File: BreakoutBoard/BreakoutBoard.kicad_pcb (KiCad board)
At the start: 2 copper layers, 49.5 x 53.3 mm, 32 parts, among them J1 addon_conn, J2 Power_top, J3 Power_bottom, J4 Conn_01x09, J5 Conn_01x10

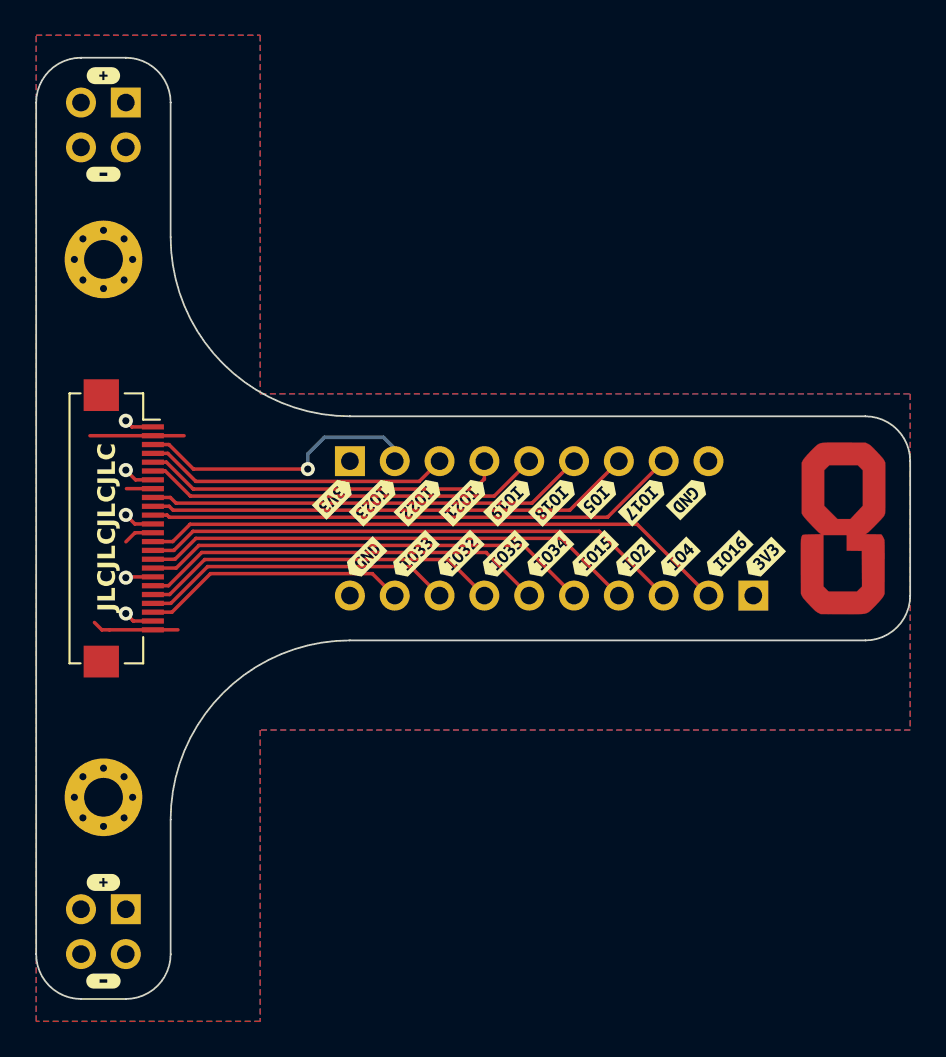
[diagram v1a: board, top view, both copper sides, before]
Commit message: Adapts breakout board to changes in the addon connector
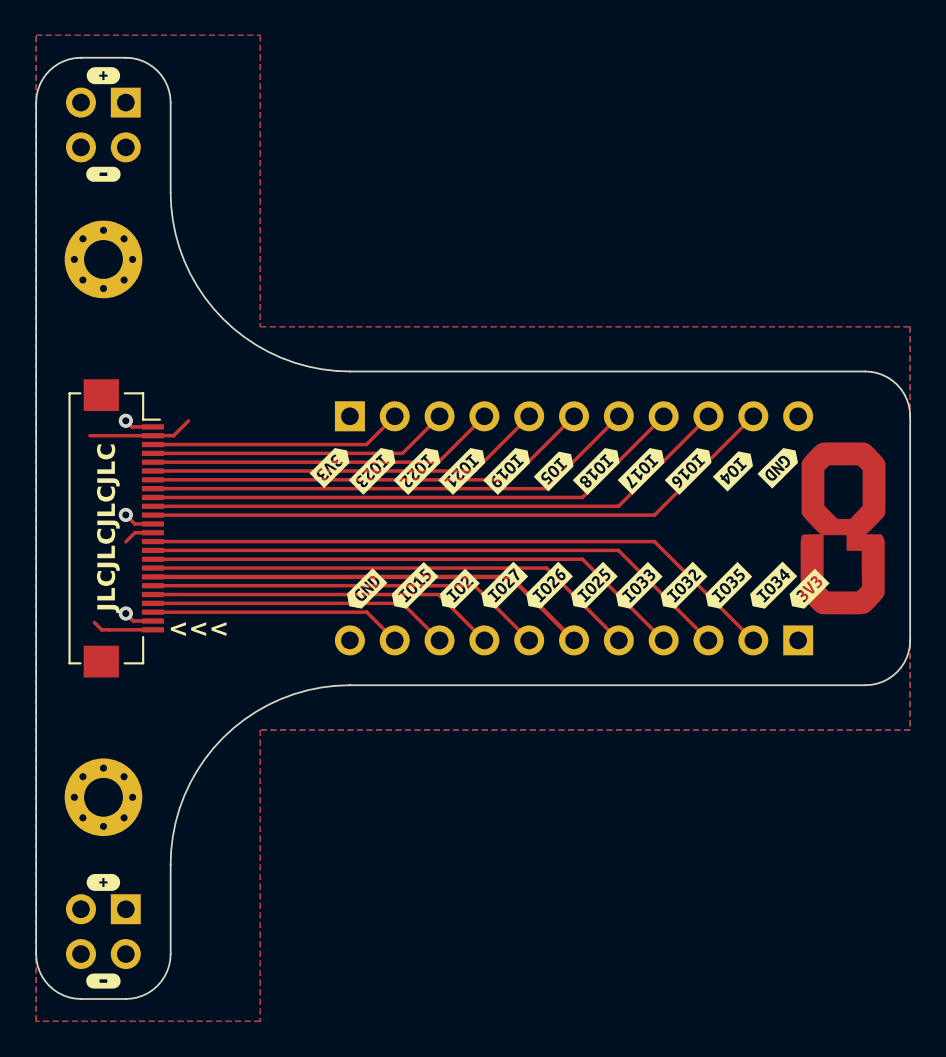
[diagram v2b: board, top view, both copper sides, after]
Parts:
- removed kibuzzard-6259454A: G***, kibuzzard-6259454A
- removed kibuzzard-6259454F: G***, kibuzzard-6259454F
- removed kibuzzard-62594553: G***, kibuzzard-62594553
- removed kibuzzard-62599743: G***, kibuzzard-62599743
- added kibuzzard-62829C43: G***, kibuzzard-62829C43, F.Cu at (164.1, 95.7)
- added kibuzzard-62829C54: G***, kibuzzard-62829C54, F.Cu at (166.6, 95.7)
- added kibuzzard-62829CE0: G***, kibuzzard-62829CE0, F.Cu at (158.5, 102.4)
- added kibuzzard-62829D15: G***, kibuzzard-62829D15, F.Cu at (150.9, 102.6)
- added kibuzzard-62829D2F: G***, kibuzzard-62829D2F, F.Cu at (153.4, 102.4)
- added kibuzzard-62829D34: G***, kibuzzard-62829D34, F.Cu at (156.0, 102.4)
- added kibuzzard-62829E35: G***, kibuzzard-62829E35, B.Cu at (156.2, 99.1)
- J1: footprint GameOver:TXGA_FFC05036-24SBD113W5M_1x24_P0.50mm_Horizontal -> GameOver:Addon_conn_TXGA_FFC05036-24SBD113W5M_1x24_P0.50mm_Horizontal
- J4: value Conn_01x09 -> Conn_01x11; footprint Connector_PinHeader_2.54mm:PinHeader_1x09_P2.54mm_Vertical -> Connector_PinHeader_2.54mm:PinHeader_1x11_P2.54mm_Vertical
- J5: value Conn_01x10 -> Conn_01x11; footprint Connector_PinHeader_2.54mm:PinHeader_1x10_P2.54mm_Vertical -> Connector_PinHeader_2.54mm:PinHeader_1x11_P2.54mm_Vertical
- moved kibuzzard-6259453E 12.8 mm to (166.1, 102.4)
- moved kibuzzard-62594542 12.8 mm to (168.7, 102.4)
- moved kibuzzard-62594532 12.8 mm to (161.0, 102.4)
- moved kibuzzard-6259453A 12.8 mm to (163.6, 102.4)
- moved kibuzzard-62594546 10.4 mm to (148.3, 102.4)
- moved kibuzzard-62594508 5.51 mm to (169.2, 95.5)
- moved J5 3.59 mm to (170.2, 105.4)
- moved kibuzzard-625944FA 3.12 mm to (158.9, 95.7)
- moved kibuzzard-62594559 3.06 mm to (170.7, 102.6)
- moved kibuzzard-625944FF 2.90 mm to (156.5, 95.7)
- moved J4 2.54 mm to (144.8, 92.7)
- moved kibuzzard-6259452C 1.82 mm to (145.6, 102.6)
- moved kibuzzard-625944F4 1.81 mm to (143.8, 95.5)
- moved kibuzzard-625944D4 1.80 mm to (153.8, 95.7)
- moved kibuzzard-625944DF 1.80 mm to (151.3, 95.7)
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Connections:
- J1 pad 10: Net-(J1-IO5) -> Net-(J1-IO16)
- J1 pad 11: Net-(J1-IO17) -> Net-(J1-IO4)
- J1 pad 18: GND -> Net-(J1-IO25)
- J1 pad 19: Net-(J1-IO34) (its old number) -> Net-(J1-IO26)
- J1 pad 20: Net-(J1-IO35) (its old number) -> Net-(J1-IO27)
- J1 pad 21: Net-(J1-IO32) (its old number) -> Net-(J1-IO2)
- J1 pad 22: Net-(J1-IO33) (its old number) -> Net-(J1-IO15)
- J1 pad 7: GND -> Net-(J1-IO5)
- J1 pad 8: +3V3 -> Net-(J1-IO18)
- J1 pad 9: Net-(J1-IO18) -> Net-(J1-IO17)
- J4 pad 6: Net-(J1-IO18) -> Net-(J1-IO5)
- J4 pad 7: Net-(J1-IO5) -> Net-(J1-IO18)
- J4 pad 9: GND -> Net-(J1-IO16)
- J5 pad 10: GND -> Net-(J1-IO15)
- J5 pad 6: Net-(J1-IO34) (its old number) -> Net-(J1-IO25)
- J5 pad 7: Net-(J1-IO35) (its old number) -> Net-(J1-IO26)
- J5 pad 8: Net-(J1-IO32) (its old number) -> Net-(J1-IO27)
- J5 pad 9: Net-(J1-IO33) (its old number) -> Net-(J1-IO2)
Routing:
- net Net-(J1-IO4): track 0.00 -> 36.3 mm
- net Net-(J1-IO16): track 0.00 -> 33.6 mm
- net Net-(J1-IO25): track 0.00 -> 25.4 mm
- net Net-(J1-IO34) (its old number): track 23.1 -> 0.00 mm
- net Net-(J1-IO26): track 0.00 -> 22.6 mm
- net Net-(J1-IO35) (its old number): track 20.5 -> 0.00 mm
- net Net-(J1-IO27): track 0.00 -> 19.9 mm
- net Net-(J1-IO32) (its old number): track 17.8 -> 0.00 mm
- net Net-(J1-IO2): track 0.00 -> 17.1 mm
- net Net-(J1-IO33) (its old number): track 15.1 -> 0.00 mm
- net Net-(J1-IO15): track 0.00 -> 14.4 mm
- net GND: track 8.45 -> 5.14 mm, vias 5 -> 3
- net Net-(J1-IO18): track 25.0 -> 28.1 mm
- net Net-(J1-IO34): track 33.6 -> 36.3 mm
- net Net-(J1-IO35): track 30.9 -> 33.6 mm
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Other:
- outline, holes or cut-outs redrawn

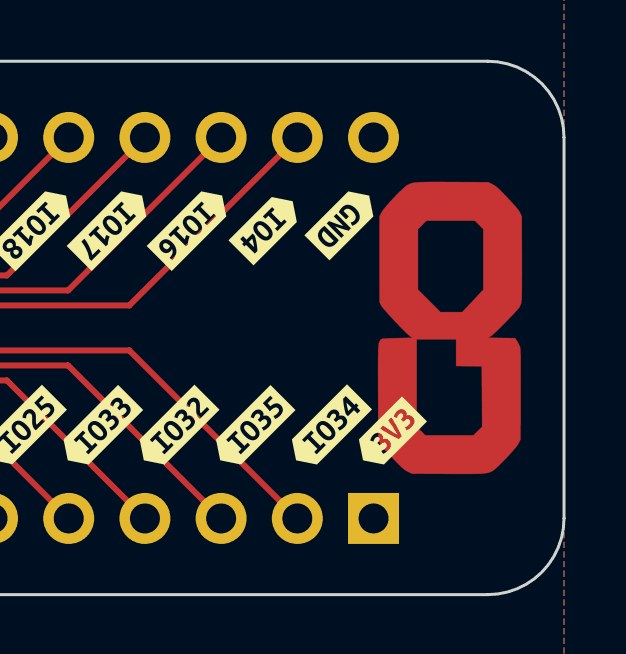
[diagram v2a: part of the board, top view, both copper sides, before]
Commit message: Adds logo to breakout board schematics
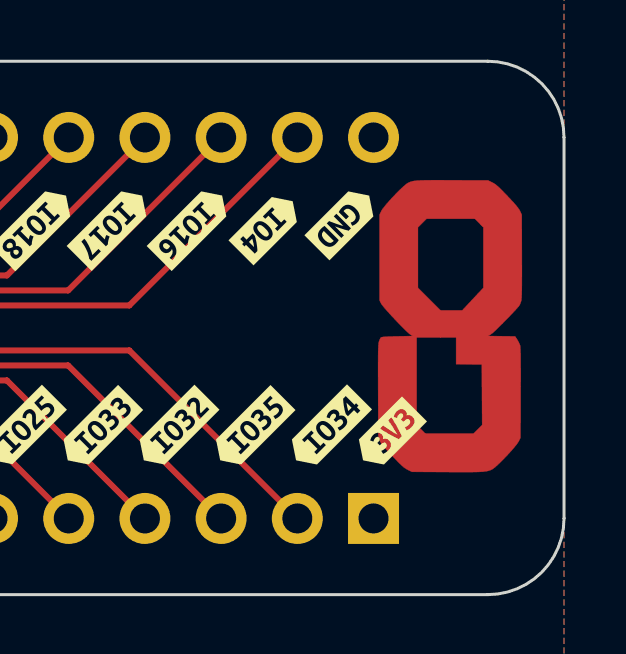
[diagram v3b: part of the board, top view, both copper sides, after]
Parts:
- removed Ref**: Val**, GameOver:logo_fcu
- added LOGO1: GameOver_logo, GameOver:logo_fcu, F.Cu at (172.7, 99.0)

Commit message: Updates all add-on boards with fix introduced in 692041
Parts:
- moved kibuzzard-625944FF 2.64 mm to (159.1, 95.5)
- moved kibuzzard-625944FA 2.56 mm to (156.3, 95.8)

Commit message: Update version label on PCBs to 1.0
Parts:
- removed kibuzzard-62829E35: G***, kibuzzard-62829E35
- added kibuzzard-63029CFF: G***, kibuzzard-63029CFF, B.Cu at (156.2, 99.1)
